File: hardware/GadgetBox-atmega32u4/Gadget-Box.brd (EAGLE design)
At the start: 93.5 x 53.5 mm, 44 parts, among them U1 MCP73831T-2ACI/OT, U2 AP2112-3.3, U3 ATMEGA32U4-XUAU, U4 ATMEGA32U4-XUMU, X1 CRYSTAL-0500290P1, X100 JSTPH

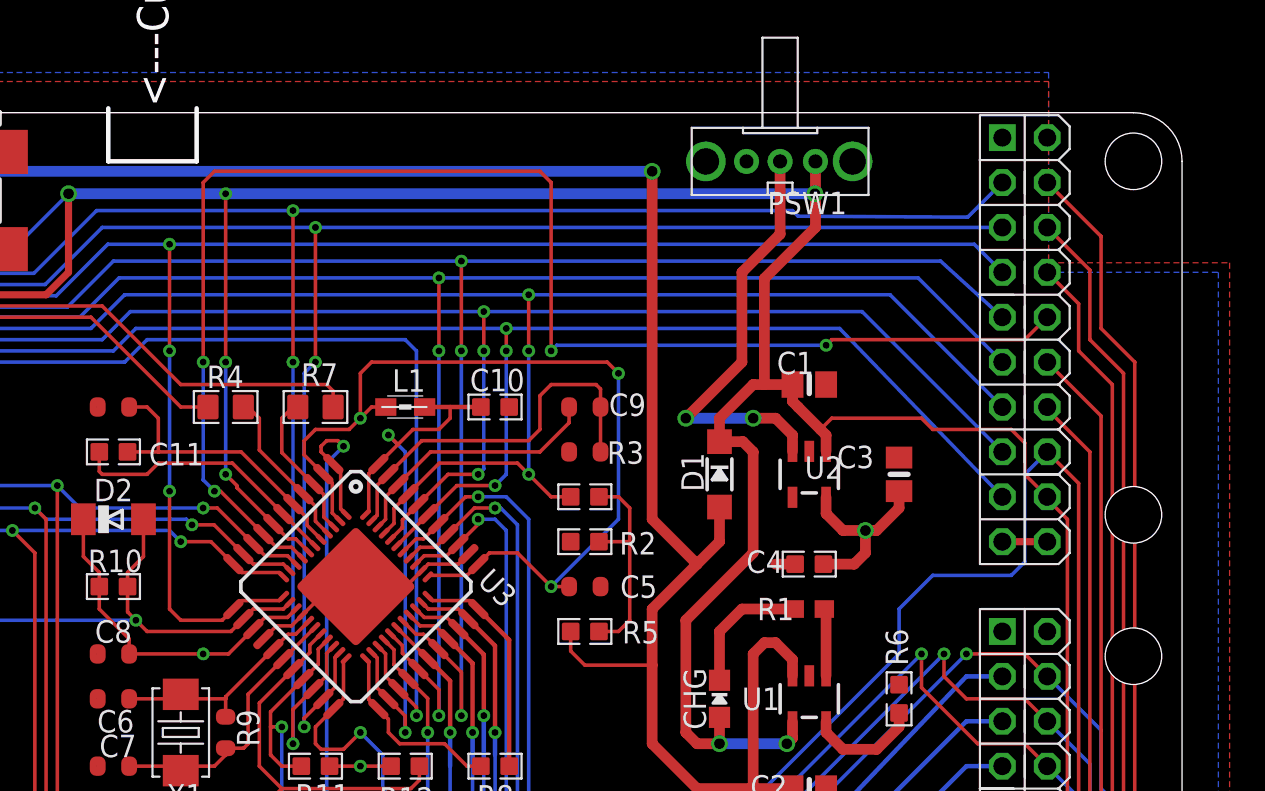
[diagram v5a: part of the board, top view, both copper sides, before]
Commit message: Added top silkscreen to layer 200.
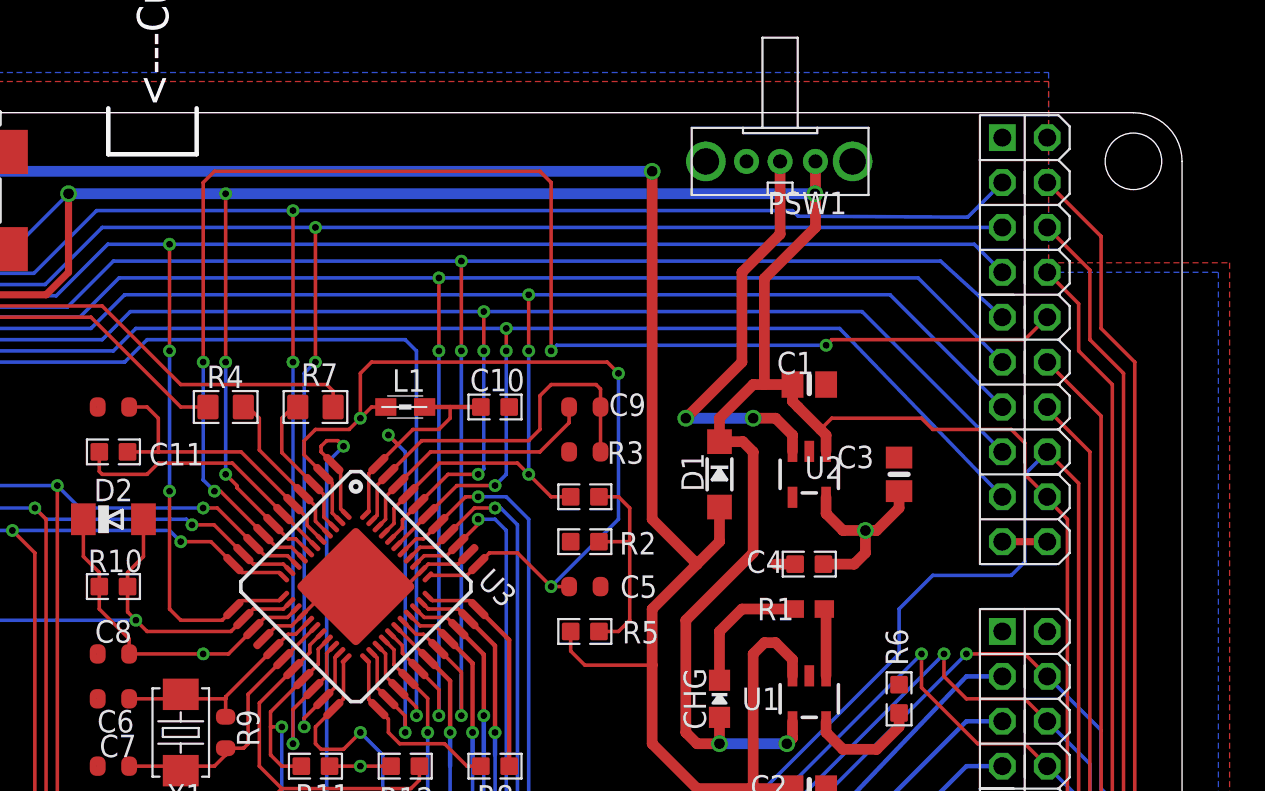
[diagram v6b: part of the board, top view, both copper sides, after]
